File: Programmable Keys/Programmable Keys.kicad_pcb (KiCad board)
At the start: 2 copper layers, 76.2 x 57.1 mm, 20 parts, among them J1 Conn_01x19_Female, J2 Conn_01x19_Male

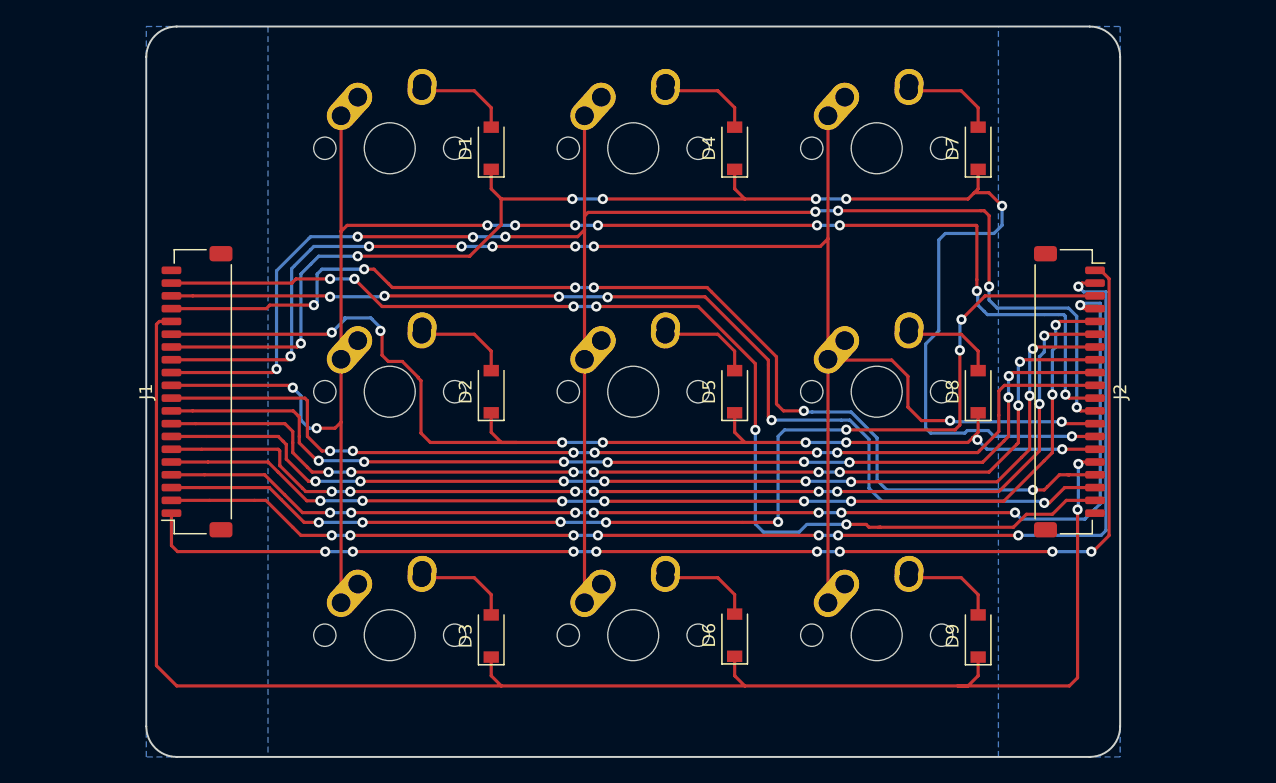
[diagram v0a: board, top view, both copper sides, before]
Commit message: Updated connectors + added mounting holes
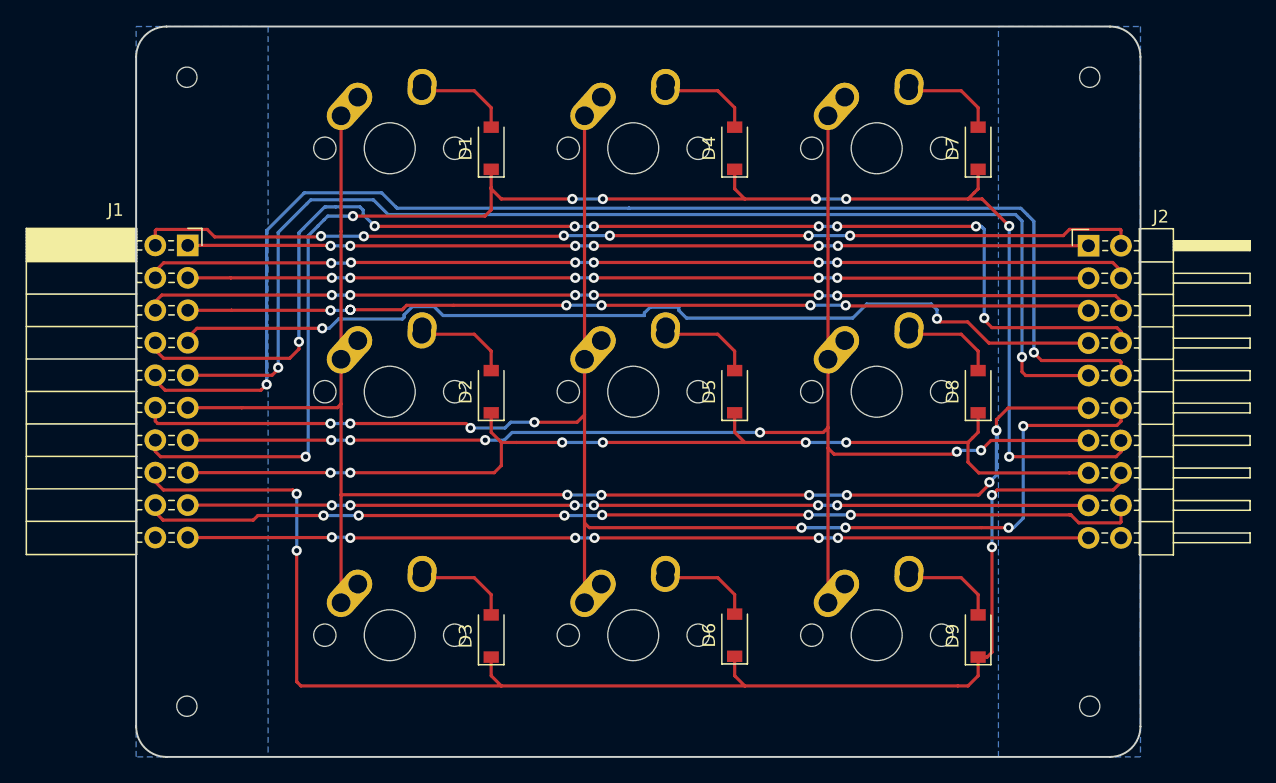
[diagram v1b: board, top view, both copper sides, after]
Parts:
- J1: value Conn_01x19_Female -> Conn_02x10_Counter_Clockwise; footprint Connector_JST:JST_SH_SM20B-SRSS-TB_1x20-1MP_P1.00mm_Horizontal -> Connector_PinSocket_2.54mm:PinSocket_2x10_P2.54mm_Horizontal
- J2: value Conn_01x19_Male -> Conn_02x10_Counter_Clockwise; footprint Connector_JST:JST_SH_SM20B-SRSS-TB_1x20-1MP_P1.00mm_Horizontal -> Connector_PinHeader_2.54mm:PinHeader_2x10_P2.54mm_Horizontal
- moved J2 11.5 mm to (222.2, 69.5), turned to 0 degrees
- moved J1 11.5 mm to (151.7, 69.5), turned to 0 degrees
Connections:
- J1 pad 20: (no net) -> unconnected-(J1-Pad20)
- J2 pad 20: (no net) -> unconnected-(J2-Pad20)
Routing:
- net +5V: track 98.1 -> 70.5 mm, vias 8 -> 6
- net COL7: track 79.7 -> 102.3 mm, vias 6 -> 2
- net COL0: track 89.5 -> 70.5 mm, vias 8 -> 6
- net GND: track 89.3 -> 70.5 mm
- net VCC: track 96.8 -> 78.5 mm, vias 8 -> 6
- net COL1: track 93.6 -> 77.2 mm, vias 8 -> 6
- net ROW8: track 86.7 -> 70.5 mm
- net ROW7: track 127.8 -> 112.1 mm, vias 2 -> 4
- net COL2: track 85.1 -> 70.8 mm, vias 8 -> 7
- net COL6: track 80.8 -> 95.0 mm, vias 8 -> 2
- net COL5: track 82.1 -> 95.9 mm
- net COL10: track 121.8 -> 109.7 mm, vias 8 -> 6
- net COL8: track 126.0 -> 114.2 mm, vias 10 -> 6
- net COL9: track 134.3 -> 124.2 mm
- net COL4: track 83.2 -> 75.3 mm, vias 8 -> 2
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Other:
- board size 76.2 x 57.1 mm -> 78.6 x 57.1 mm

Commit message: Extended pcb for connectors
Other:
- board size 78.6 x 57.1 mm -> 83.3 x 57.1 mm
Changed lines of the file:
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@@
     )
   )
-  (gr_arc (start 150.01875 109.5375) (mid 148.333407 108.841578) (end 147.6375 107.15625) (layer "Edge.Cuts") (width 0.15))
+  (gr_arc (start 147.6375 109.5375) (mid 145.953702 108.840048) (end 145.25625 107.15625) (layer "Edge.Cuts") (width 0.15))
   (gr_circle (center 151.60625 105.56875) (end 152.4 105.56875) (layer "Edge.Cuts") (width 0.1) (fill none))
-  (gr_line (start 150.01875 52.3875) (end 223.8375 52.3875) (layer "Edge.Cuts") (width 0.15))
+  (gr_arc (start 226.21875 52.3875) (mid 227.902548 53.084952) (end 228.6 54.76875) (layer "Edge.Cuts") (width 0.15))
+  (gr_line (start 147.6375 52.3875) (end 226.21875 52.3875) (layer "Edge.Cuts") (width 0.15))
   (gr_circle (center 222.25 105.56875) (end 223.04375 105.56875) (layer "Edge.Cuts") (width 0.1) (fill none))
-  (gr_arc (start 226.21875 107.15625) (mid 225.52128 108.840016) (end 223.8375 109.5375) (layer "Edge.Cuts") (width 0.15))
-  (gr_line (start 147.6375 107.15625) (end 147.6375 54.76875) (layer "Edge.Cuts") (width 0.15))
-  (gr_line (start 150.01875 109.5375) (end 223.8375 109.5375) (layer "Edge.Cuts") (width 0.15))
+  (gr_line (start 145.25625 107.15625) (end 145.25625 54.76875) (layer "Edge.Cuts") (width 0.15))
+  (gr_line (start 147.6375 109.5375) (end 226.21875 109.5375) (layer "Edge.Cuts") (width 0.15))
   (gr_circle (center 222.25 56.35625) (end 222.25 55.5625) (layer "Edge.Cuts") (width 0.1) (fill none))
-  (gr_arc (start 223.8375 52.3875) (mid 225.521316 53.084949) (end 226.21875 54.76875) (layer "Edge.Cuts") (width 0.15))
-  (gr_line (start 226.21875 54.76875) (end 226.21875 107.15625) (layer "Edge.Cuts") (width 0.15))
+  (gr_arc (start 228.6 107.15625) (mid 227.902548 108.840048) (end 226.21875 109.5375) (layer "Edge.Cuts") (width 0.15))
+  (gr_line (start 228.6 54.76875) (end 228.6 107.15625) (layer "Edge.Cuts") (width 0.15))
   (gr_circle (center 151.60625 56.35625) (end 151.60625 55.5625) (layer "Edge.Cuts") (width 0.1) (fill none))
-  (gr_arc (start 147.6375 54.76875) (mid 148.33497 53.084984) (end 150.01875 52.3875) (layer "Edge.Cuts") (width 0.15))
+  (gr_arc (start 145.25625 54.76875) (mid 145.953702 53.084952) (end 147.6375 52.3875) (layer "Edge.Cuts") (width 0.15))
   (segment (start 195.2625 65.88125) (end 184.15 65.88125) (width 0.25) (layer "F.Cu") (net 1))
   (segment (start 215.95 68) (end 213.83125 65.88125) (width 0.25) (layer "F.Cu") (net 1))
@@
     (polygon
       (pts
-        (xy 226.21875 109.5375)
+        (xy 228.6 109.5375)
         (xy 215.10625 109.5375)
         (xy 215.10625 52.3875)
-        (xy 226.21875 52.3875)
+        (xy 228.6 52.3875)
       )
     )
@@
       (pts
         (xy 157.95625 109.5375)
-        (xy 147.6375 109.5375)
-        (xy 147.6375 52.3875)
+        (xy 145.25625 109.5375)
+        (xy 145.25625 52.3875)
         (xy 157.95625 52.3875)
       )
